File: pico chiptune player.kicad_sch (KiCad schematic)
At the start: 24 parts, among them J1 MicroSD, J2 Speaker Out, SW1 Play / Pause, SW2 Next, SW3 Previous, U1 AY-3-8910, U2 PAM8302AAS, U3 0.96"OLED_I2C

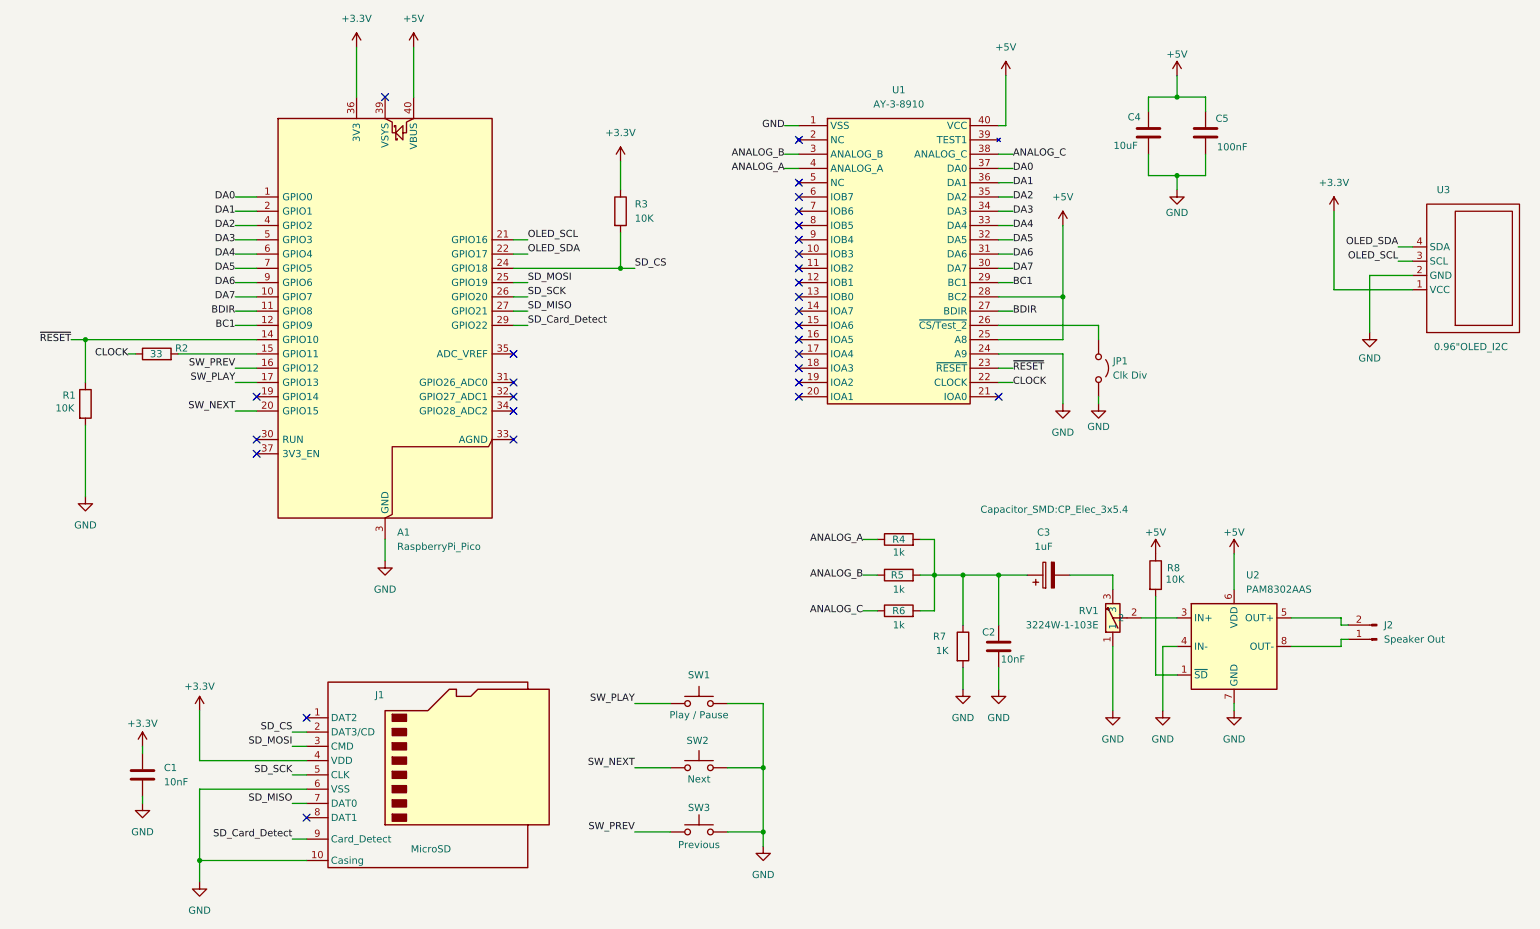
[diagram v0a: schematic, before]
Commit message: pcb, dru: update silk text sizes to >=0.8mm for DRC compliance and add JLCPCB design rules
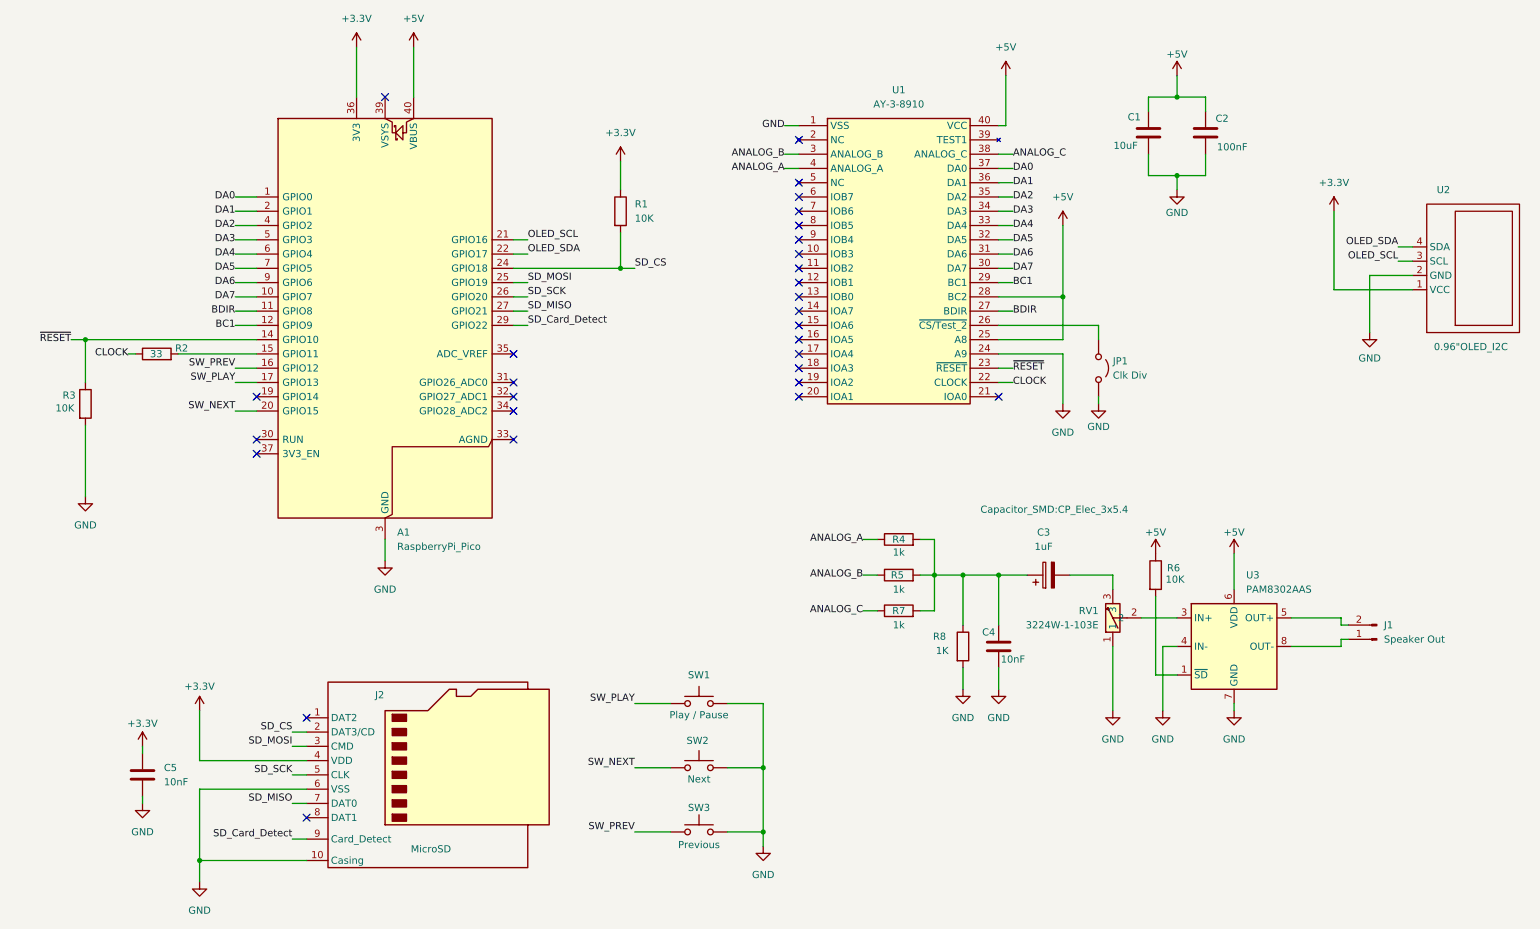
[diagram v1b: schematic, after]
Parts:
- renumbered C4 to C1, C5 to C2, C2 to C4, C1 to C5, J2 to J1, J1 to J2, R3 to R1, R1 to R3, R8 to R6, R6 to R7, R7 to R8, U3 to U2, U2 to U3

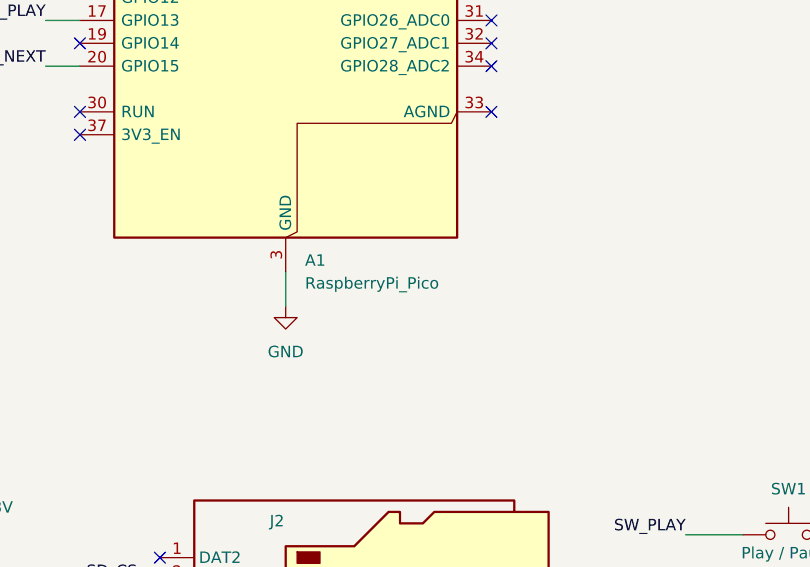
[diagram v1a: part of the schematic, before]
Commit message: fix(dru): update JLCPCB custom design rules syntax for KiCad 10 compliance
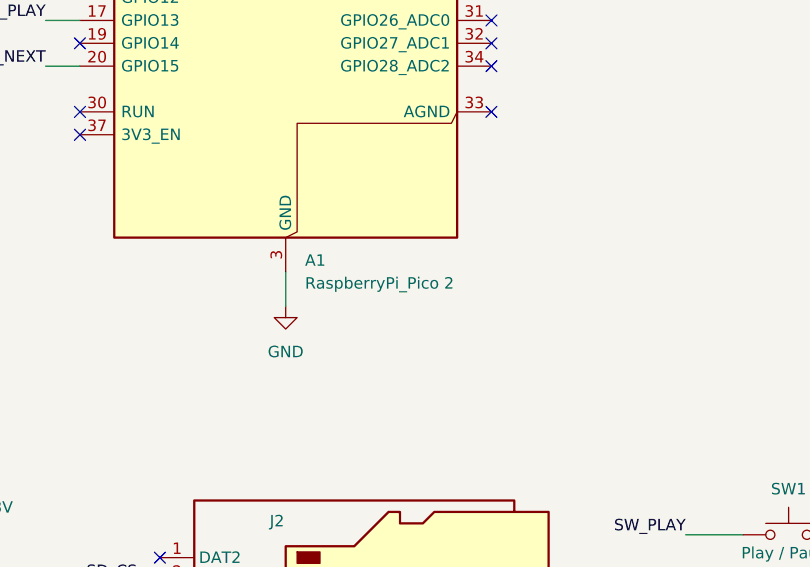
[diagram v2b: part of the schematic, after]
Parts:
- A1: value RaspberryPi_Pico -> RaspberryPi_Pico 2
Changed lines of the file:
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@@
 			)
 		)
-		(property "Value" "RaspberryPi_Pico"
+		(property "Value" "RaspberryPi_Pico 2"
 			(at 78.3433 111.76 0)
 			(show_name no)

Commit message: sch, bom: add LCSC Part # numbers for JLCPCB SMT PCBA assembly
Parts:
- A1: LCSC Part # (none) -> C17414; now left out of the parts list
- C1: LCSC Part # (none) -> C15850
- C2: LCSC Part # (none) -> C81348
- C3, R5, SW1: LCSC Part # (none) -> C17513
- C5: LCSC Part # (none) -> C17414
- R1: LCSC Part # (none) -> C17631
- R4: LCSC Part # (none) -> C12437
- RV1: LCSC Part # C81348 -> C12740
- SW2: LCSC Part # (none) -> C114217
- SW3: LCSC Part # (none) -> C12740
- U1: now left out of the parts list
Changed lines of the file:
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@@
 		(pin "2"
 		)
+		(property "LCSC Part #" "C17513"
+			(at 0 0 0)
+			(hide yes)
+			(show_name no)
+			(do_not_autoplace no)
+			(effects
+				(font
+					(size 1.27 1.27)
+				)
+			)
+		)
 		(instances
 			(project "pico chiptune player"
@@
 		(pin "1"
 		)
+		(property "LCSC Part #" "C15848"
+			(at 0 0 0)
+			(hide yes)
+			(show_name no)
+			(do_not_autoplace no)
+			(effects
+				(font
+					(size 1.27 1.27)
+				)
+			)
+		)
 		(instances
 			(project "pico chiptune player"
@@
 		(pin "1"
 		)
+		(property "LCSC Part #" "C17513"
+			(at 0 0 0)
+			(hide yes)
+			(show_name no)
+			(do_not_autoplace no)
+			(effects
+				(font
+					(size 1.27 1.27)
+				)
+			)
+		)
 		(instances
 			(project "pico chiptune player"
@@
 		(pin "2"
 		)
+		(property "LCSC Part #" "C12437"
+			(at 0 0 0)
+			(hide yes)
+			(show_name no)
+			(do_not_autoplace no)
+			(effects
+				(font
+					(size 1.27 1.27)
+				)
+			)
+		)
 		(instances
 			(project "pico chiptune player"
@@
 		(pin "1"
 		)
+		(property "LCSC Part #" "C49678"
+			(at 0 0 0)
+			(hide yes)
+			(show_name no)
+			(do_not_autoplace no)
+			(effects
+				(font
+					(size 1.27 1.27)
+				)
+			)
+		)
 		(instances
 			(project "pico chiptune player"
@@
 		(pin "2"
 		)
+		(property "LCSC Part #" "C81348"
+			(at 0 0 0)
+			(hide yes)
+			(show_name no)
+			(do_not_autoplace no)
+			(effects
+				(font
+					(size 1.27 1.27)
+				)
+			)
+		)
 		(instances
 			(project "pico chiptune player"
@@
 			)
 		)
-		(property "LCSC Part #" "C81348"
+		(property "LCSC Part #" "C12740"
 			(at 205.74 124.46 0)
 			(hide yes)
@@
 		(pin "2"
 		)
+		(property "LCSC Part #" "C114217"
+			(at 0 0 0)
+			(hide yes)
+			(show_name no)
+			(do_not_autoplace no)
+			(effects
+				(font
+					(size 1.27 1.27)
+				)
+			)
+		)
 		(instances
 			(project "pico chiptune player"
@@
 		(pin "2"
 		)
+		(property "LCSC Part #" "C15850"
+			(at 0 0 0)
+			(hide yes)
+			(show_name no)
+			(do_not_autoplace no)
+			(effects
+				(font
+					(size 1.27 1.27)
+				)
+			)
+		)
 		(instances
 			(project "pico chiptune player"
@@
 		(pin "1"
 		)
+		(property "LCSC Part #" "C17414"
+			(at 0 0 0)
+			(hide yes)
+			(show_name no)
+			(do_not_autoplace no)
+			(effects
+				(font
+					(size 1.27 1.27)
+				)
+			)
+		)
+		(property "LCSC Part #" "C17631"
+			(at 0 0 0)
+			(hide yes)
+			(show_name no)
+			(do_not_autoplace no)
+			(effects
+				(font
+					(size 1.27 1.27)
+				)
+			)
+		)
 		(instances
 			(project "pico chiptune player"
@@
 		(body_style 1)
 		(exclude_from_sim no)
-		(in_bom yes)
-		(on_board yes)
+		(in_bom no)
+		(on_board no)
 		(in_pos_files yes)
 		(dnp no)
@@
 		(pin "1"
 		)
+		(property "LCSC Part #" "C17513"
+			(at 0 0 0)
+			(hide yes)
+			(show_name no)
+			(do_not_autoplace no)
+			(effects
+				(font
+					(size 1.27 1.27)
+				)
+			)
+		)
 		(instances
 			(project "pico chiptune player"
@@
 		(pin "1"
 		)
+		(property "LCSC Part #" "C12740"
+			(at 0 0 0)
+			(hide yes)
+			(show_name no)
+			(do_not_autoplace no)
+			(effects
+				(font
+					(size 1.27 1.27)
+				)
+			)
+		)
 		(instances
 			(project "pico chiptune player"
@@
 		(pin "1"
 		)
+		(property "LCSC Part #" "C17513"
+			(at 0 0 0)
+			(hide yes)
+			(show_name no)
+			(do_not_autoplace no)
+			(effects
+				(font
+					(size 1.27 1.27)
+				)
+			)
+		)
 		(instances
 			(project "pico chiptune player"
@@
 		(pin "1"
 		)
+		(property "LCSC Part #" "C12740"
+			(at 0 0 0)
+			(hide yes)
+			(show_name no)
+			(do_not_autoplace no)
+			(effects
+				(font
+					(size 1.27 1.27)
+				)
+			)
+		)
 		(instances
 			(project "pico chiptune player"
@@
 		(pin "1"
 		)
+		(property "LCSC Part #" "C12740"
+			(at 0 0 0)
+			(hide yes)
+			(show_name no)
+			(do_not_autoplace no)
+			(effects
+				(font
+					(size 1.27 1.27)
+				)
+			)
+		)
 		(instances
 			(project "pico chiptune player"
@@
 		(pin "1"
 		)
+		(property "LCSC Part #" "C1710"
+			(at 0 0 0)
+			(hide yes)
+			(show_name no)
+			(do_not_autoplace no)
+			(effects
+				(font
+					(size 1.27 1.27)
+				)
+			)
+		)
+		(property "LCSC Part #" "C17414"
+			(at 0 0 0)
+			(hide yes)
+			(show_name no)
+			(do_not_autoplace no)
+			(effects
+				(font
+					(size 1.27 1.27)
+				)
+			)
+		)
 		(instances
 			(project "pico chiptune player"
@@
 		(body_style 1)
 		(exclude_from_sim no)
-		(in_bom yes)
-		(on_board yes)
+		(in_bom no)
+		(on_board no)
 		(in_pos_files yes)
 		(dnp no)
@@
 		(pin "38"
 		)
+		(property "LCSC Part #" "C17414"
+			(at 0 0 0)
+			(hide yes)
+			(show_name no)
+			(do_not_autoplace no)
+			(effects
+				(font
+					(size 1.27 1.27)
+				)
+			)
+		)
 		(instances

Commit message: sch: add LCSC property fields directly to all schematic symbols
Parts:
- C2: LCSC (none) -> C81348
- C3, R5, SW1: LCSC (none) -> C17513
- R2: LCSC (none) -> C17631
- R3, R6: LCSC (none) -> C17414
- R4: LCSC (none) -> C12437
- RV1: LCSC (none) -> C12740
- SW2: LCSC (none) -> C114217
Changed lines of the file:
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@@
 			)
 		)
+		(property "LCSC" "C17513"
+			(at 0 0 0)
+			(hide yes)
+			(show_name no)
+			(do_not_autoplace no)
+			(effects
+				(font
+					(size 1.27 1.27)
+				)
+			)
+		)
 		(instances
 			(project "pico chiptune player"
@@
 			)
 		)
+		(property "LCSC" "C15848"
+			(at 0 0 0)
+			(hide yes)
+			(show_name no)
+			(do_not_autoplace no)
+			(effects
+				(font
+					(size 1.27 1.27)
+				)
+			)
+		)
 		(instances
 			(project "pico chiptune player"
@@
 			)
 		)
+		(property "LCSC" "C17513"
+			(at 0 0 0)
+			(hide yes)
+			(show_name no)
+			(do_not_autoplace no)
+			(effects
+				(font
+					(size 1.27 1.27)
+				)
+			)
+		)
 		(instances
 			(project "pico chiptune player"
@@
 			)
 		)
+		(property "LCSC" "C12437"
+			(at 0 0 0)
+			(hide yes)
+			(show_name no)
+			(do_not_autoplace no)
+			(effects
+				(font
+					(size 1.27 1.27)
+				)
+			)
+		)
 		(instances
 			(project "pico chiptune player"
@@
 			)
 		)
+		(property "LCSC" "C49678"
+			(at 0 0 0)
+			(hide yes)
+			(show_name no)
+			(do_not_autoplace no)
+			(effects
+				(font
+					(size 1.27 1.27)
+				)
+			)
+		)
 		(instances
 			(project "pico chiptune player"
@@
 			)
 		)
+		(property "LCSC" "C81348"
+			(at 0 0 0)
+			(hide yes)
+			(show_name no)
+			(do_not_autoplace no)
+			(effects
+				(font
+					(size 1.27 1.27)
+				)
+			)
+		)
 		(instances
 			(project "pico chiptune player"
@@
 		(pin "2"
 		)
+		(property "LCSC" "C12740"
+			(at 0 0 0)
+			(hide yes)
+			(show_name no)
+			(do_not_autoplace no)
+			(effects
+				(font
+					(size 1.27 1.27)
+				)
+			)
+		)
 		(instances
 			(project "pico chiptune player"
@@
 			)
 		)
+		(property "LCSC" "C114217"
+			(at 0 0 0)
+			(hide yes)
+			(show_name no)
+			(do_not_autoplace no)
+			(effects
+				(font
+					(size 1.27 1.27)
+				)
+			)
+		)
 		(instances
 			(project "pico chiptune player"
@@
 		(pin "1"
 		)
+		(property "LCSC" "C17631"
+			(at 0 0 0)
+			(hide yes)
+			(show_name no)
+			(do_not_autoplace no)
+			(effects
+				(font
+					(size 1.27 1.27)
+				)
+			)
+		)
 		(instances
 			(project "pico chiptune player"
@@
 			)
 		)
+		(property "LCSC" "C17513"
+			(at 0 0 0)
+			(hide yes)
+			(show_name no)
+			(do_not_autoplace no)
+			(effects
+				(font
+					(size 1.27 1.27)
+				)
+			)
+		)
 		(instances
 			(project "pico chiptune player"
@@
 			)
 		)
+		(property "LCSC" "C12740"
+			(at 0 0 0)
+			(hide yes)
+			(show_name no)
+			(do_not_autoplace no)
+			(effects
+				(font
+					(size 1.27 1.27)
+				)
+			)
+		)
 		(instances
 			(project "pico chiptune player"
@@
 			)
 		)
+		(property "LCSC" "C17513"
+			(at 0 0 0)
+			(hide yes)
+			(show_name no)
+			(do_not_autoplace no)
+			(effects
+				(font
+					(size 1.27 1.27)
+				)
+			)
+		)
 		(instances
 			(project "pico chiptune player"
@@
 			)
 		)
+		(property "LCSC" "C12740"
+			(at 0 0 0)
+			(hide yes)
+			(show_name no)
+			(do_not_autoplace no)
+			(effects
+				(font
+					(size 1.27 1.27)
+				)
+			)
+		)
 		(instances
 			(project "pico chiptune player"
@@
 		(pin "1"
 		)
+		(property "LCSC" "C1710"
+			(at 0 0 0)
+			(hide yes)
+			(show_name no)
+			(do_not_autoplace no)
+			(effects
+				(font
+					(size 1.27 1.27)
+				)
+			)
+		)
 		(instances
 			(project "pico chiptune player"
@@
 		(pin "2"
 		)
+		(property "LCSC" "C17414"
+			(at 0 0 0)
+			(hide yes)
+			(show_name no)
+			(do_not_autoplace no)
+			(effects
+				(font
+					(size 1.27 1.27)
+				)
+			)
+		)
 		(instances
 			(project "pico chiptune player"
@@
 		(pin "1"
 		)
+		(property "LCSC" "C17414"
+			(at 0 0 0)
+			(hide yes)
+			(show_name no)
+			(do_not_autoplace no)
+			(effects
+				(font
+					(size 1.27 1.27)
+				)
+			)
+		)
 		(instances
